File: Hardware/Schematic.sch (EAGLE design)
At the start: 103 parts, among them IC1 BD5229G-TR, IC4 XC6220A331MR-G, J1 FH34SRJ-24S-0.5SH_99_, J2 SAMACSYS_PARTS_USB4110-GF-A, J3 QWIIC_RIGHT_ANGLE, J4 112A-TAAR-R03_ATTEND, Q1 20V/4.2A/52mΩ/1.4W, Q2 20V/4.2A/52mΩ/1.4W, Q3 SI1308EDL-T1-GE3, U1 W25Q512JVEIQ, U2 ESP32-C6-WROOM-1-N8, U3 DS3231SN#, U4 MAX17048G+T10

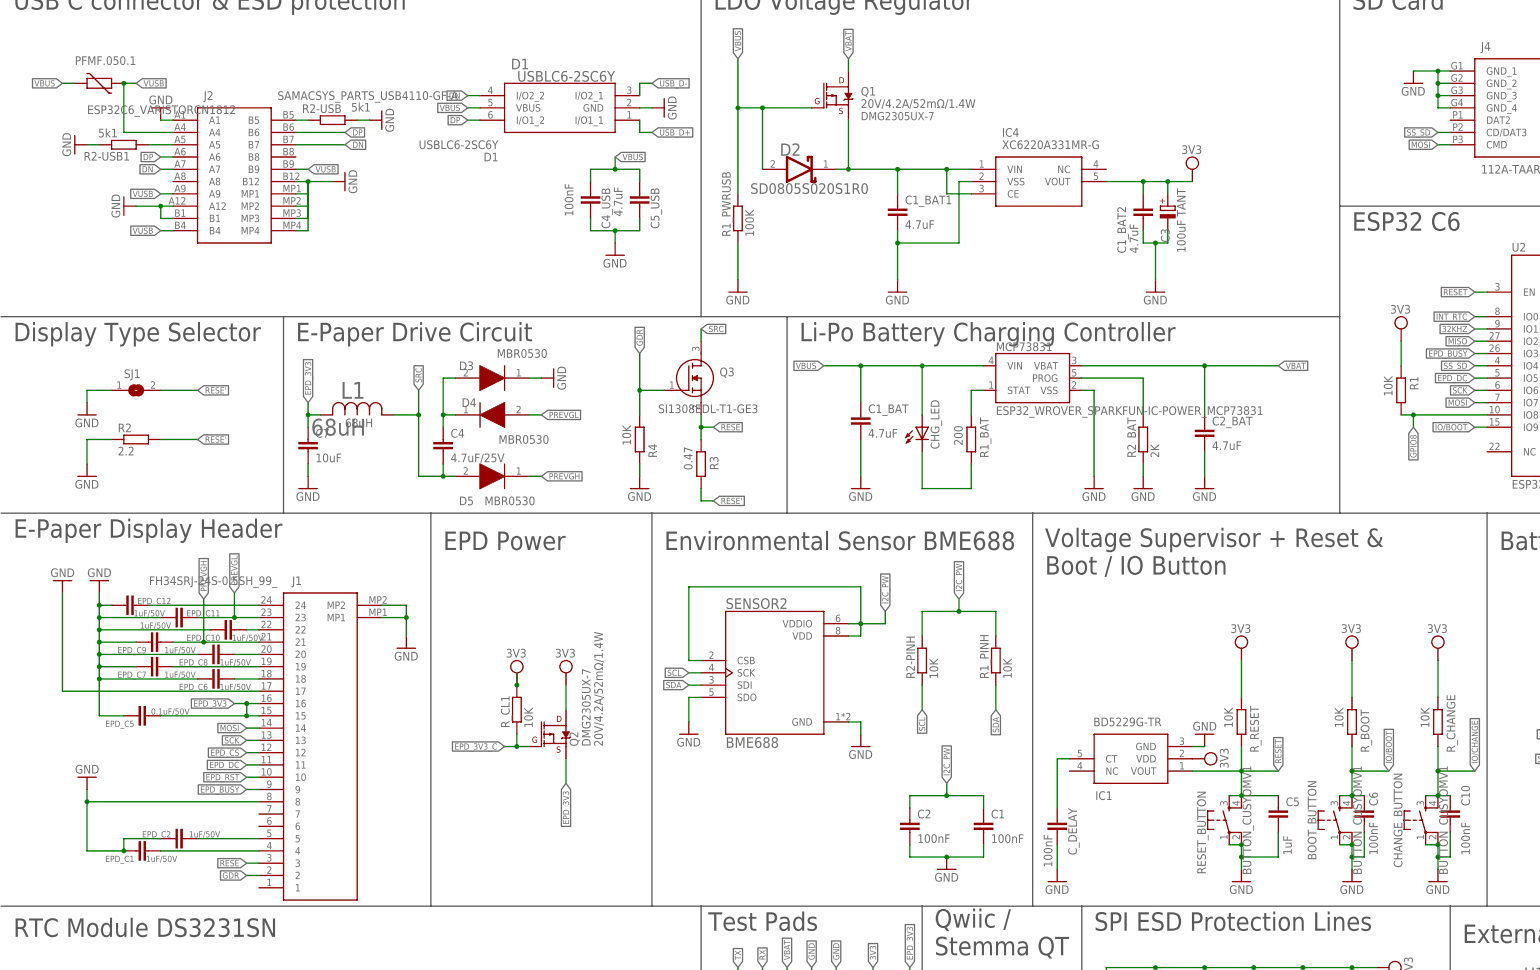
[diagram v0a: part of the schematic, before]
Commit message: Solved issues
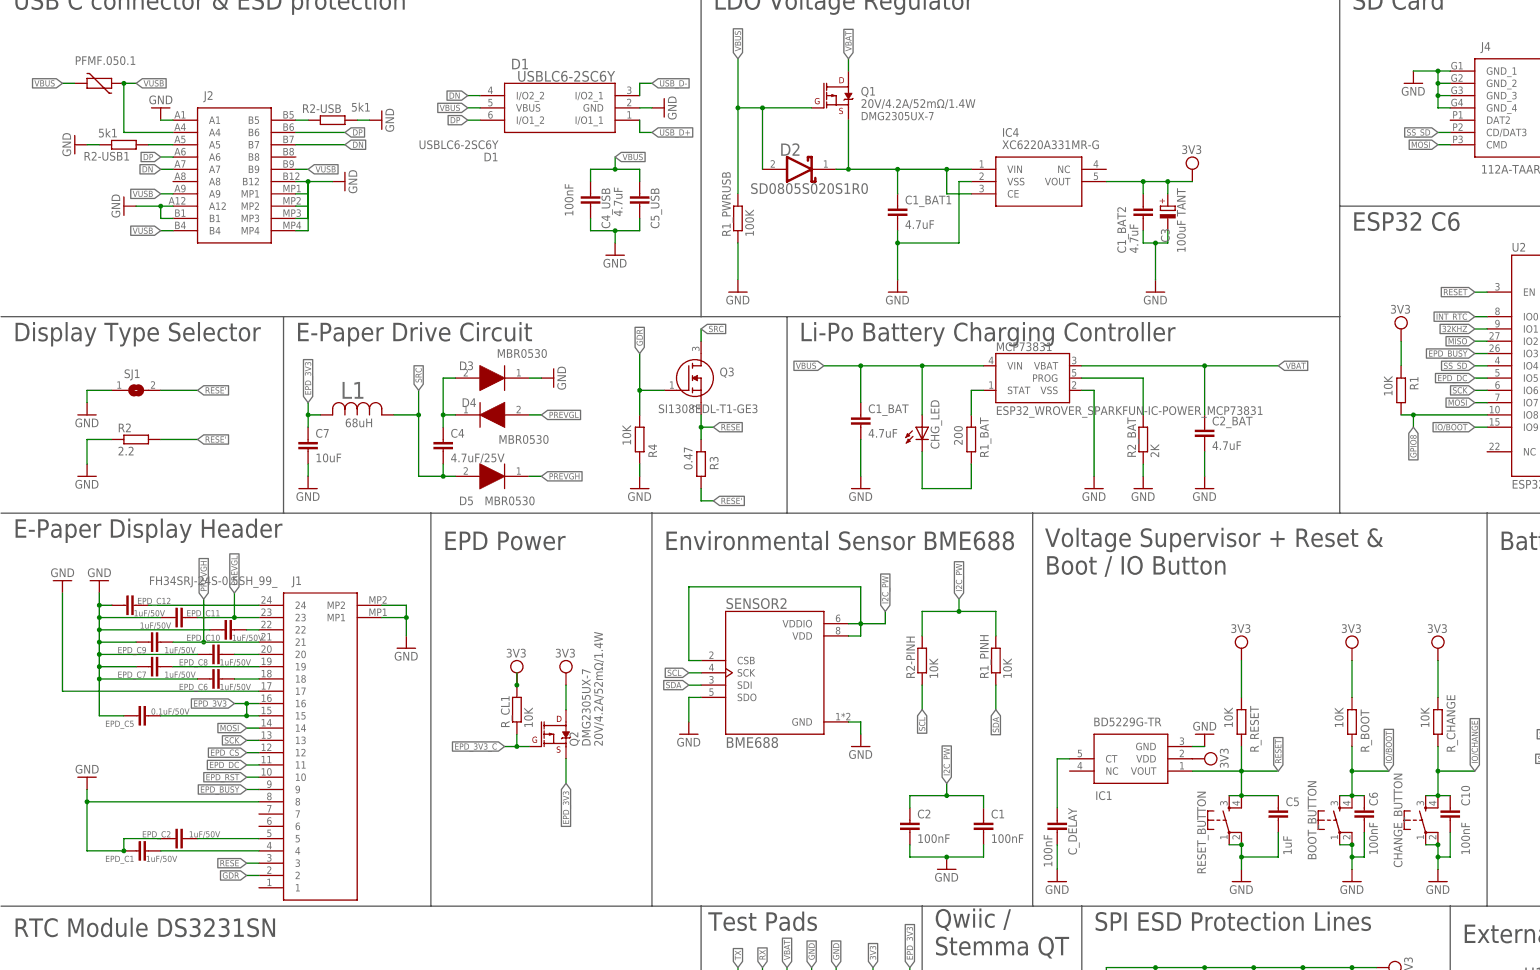
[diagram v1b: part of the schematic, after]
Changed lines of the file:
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@@
 <instance part="J2" gate="G$1" x="17.78" y="218.44" smashed="yes">
 <attribute name="NAME" x="24.13" y="223.52" size="1.778" layer="95" align="center-left"/>
-<attribute name="VALUE" x="39.37" y="223.52" size="1.778" layer="96" align="center-left"/>
 </instance>
 <instance part="GND1" gate="1" x="-2.54" y="213.36" smashed="yes" rot="R270">
@@
 <instance part="PFMF.050.1" gate="G$1" x="2.54" y="226.06" smashed="yes">
 <attribute name="NAME" x="-2.54" y="229.87" size="1.778" layer="95"/>
-<attribute name="VALUE" x="0" y="219.71" size="1.778" layer="96"/>
 </instance>
 <instance part="D1" gate="G$1" x="114.3" y="218.44" smashed="yes" rot="R180">
@@
 <instance part="RESET_BUTTON" gate="G$1" x="236.22" y="73.66" smashed="yes" rot="R90">
 <attribute name="NAME" x="231.394" y="71.12" size="1.778" layer="95" font="vector" rot="R90" align="bottom-center"/>
-<attribute name="VALUE" x="239.014" y="73.66" size="1.778" layer="96" font="vector" rot="R90" align="top-center"/>
 </instance>
 <instance part="R_RESET" gate="G$1" x="238.76" y="93.98" smashed="yes" rot="R90">
@@
 <instance part="CHANGE_BUTTON" gate="G$1" x="276.86" y="73.66" smashed="yes" rot="R90">
 <attribute name="NAME" x="272.034" y="73.66" size="1.778" layer="95" font="vector" rot="R90" align="bottom-center"/>
-<attribute name="VALUE" x="279.654" y="73.66" size="1.778" layer="96" font="vector" rot="R90" align="top-center"/>
 </instance>
 <instance part="R_CHANGE" gate="G$1" x="279.4" y="93.98" smashed="yes" rot="R90">
@@
 <instance part="BOOT_BUTTON" gate="G$1" x="259.08" y="73.66" smashed="yes" rot="R90">
 <attribute name="NAME" x="254.254" y="73.66" size="1.778" layer="95" font="vector" rot="R90" align="bottom-center"/>
-<attribute name="VALUE" x="261.874" y="73.66" size="1.778" layer="96" font="vector" rot="R90" align="top-center"/>
 </instance>
 <instance part="R_BOOT" gate="G$1" x="261.62" y="93.98" smashed="yes" rot="R90">
@@
 <attribute name="NAME" x="52.4302" y="160.8201" size="3.48" layer="95" ratio="10"/>
 <attribute name="VALOARE" x="53.34" y="154.94" size="1.778" layer="96"/>
-<attribute name="VALUE" x="46.2819" y="153.2001" size="3.48" layer="96" ratio="10"/>
 </instance>
 <instance part="C4" gate="G$1" x="73.66" y="152.4" smashed="yes">
